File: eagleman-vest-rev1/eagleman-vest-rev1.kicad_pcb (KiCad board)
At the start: 2 copper layers, 84 parts, among them P1 USB_C_Plug_USB2.0, U1 ESP32-S3-WROOM-2, U10 DRV2605LDGSR, U11 DRV2605LDGSR, U12 DRV2605LDGSR, U13 DRV2605LDGSR, U14 DRV2605LDGSR, U15 DRV2605LDGSR, U16 DRV2605LDGSR, U2 AP1117-33, U3 TCA9548APWR, U4 TCA9548APWR, U5 ESP32-S3-WROOM-1-N8, U7 DRV2605LDGSR, U8 DRV2605LDGSR, U9 DRV2605LDGSR

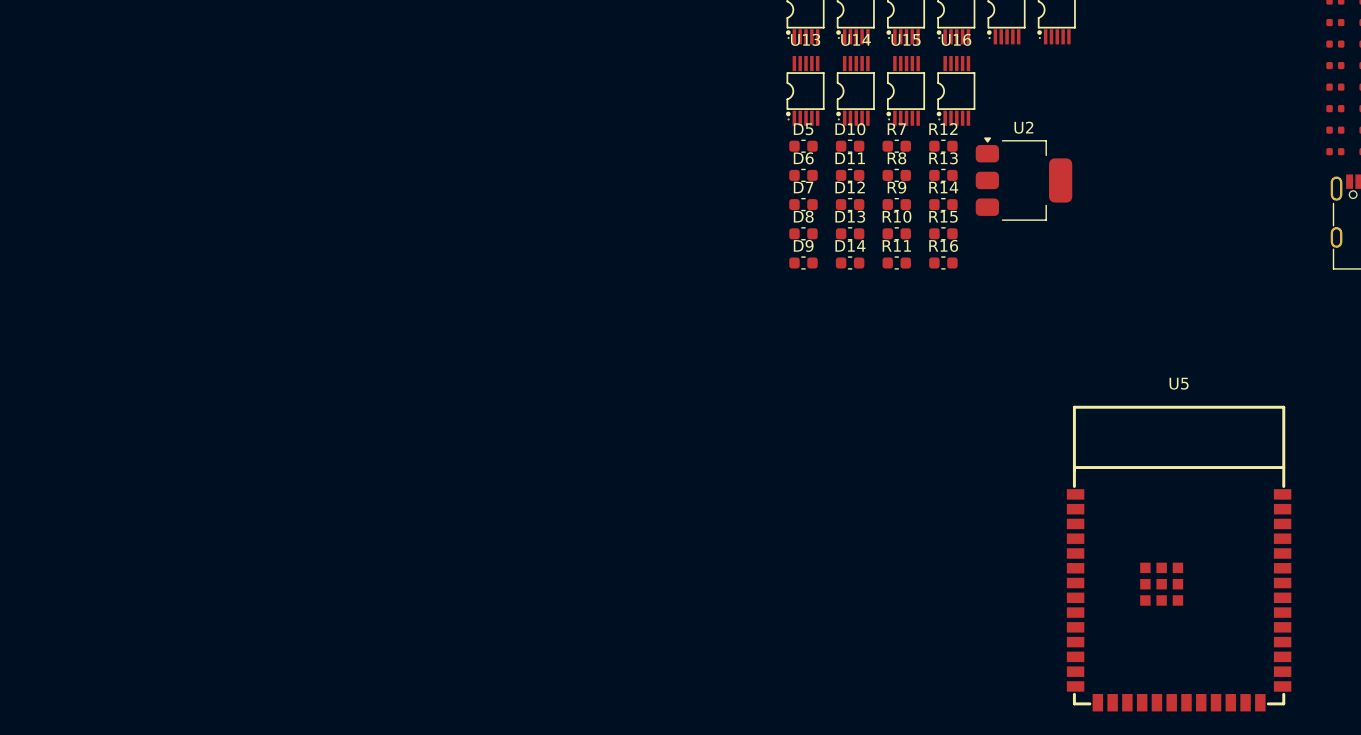
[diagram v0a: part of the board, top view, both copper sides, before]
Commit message: removed duplicate esp32 - why is its footprint not gone?
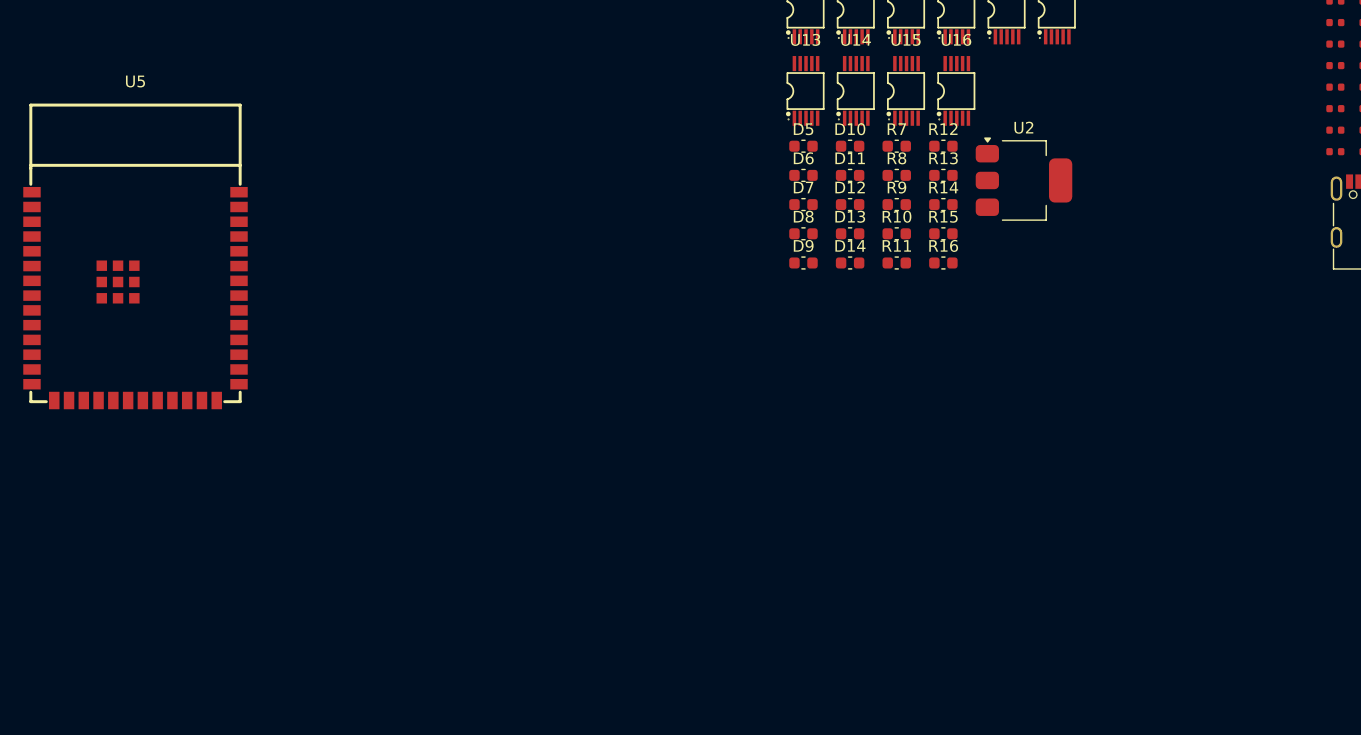
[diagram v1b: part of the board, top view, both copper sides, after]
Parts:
- moved U5 93.4 mm to (70.1, 140.6)
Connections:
- P1 pad A7: Net-(P1-D-) -> Net-(D14-A)
- U1 pad 1: Net-(U1-GND-Pad1) -> GND
- U1 pad 13: Net-(P1-D-) -> Net-(D14-A)
- U1 pad 22: unconnected-(U1-IO14-Pad22) -> /GPIOEN
- U1 pad 23: unconnected-(U1-IO21-Pad23) -> /f1-reset
- U1 pad 31: unconnected-(U1-IO38-Pad31) -> /f2-reset
- U1 pad 40: Net-(U1-GND-Pad1) -> GND
- U1 pad 41: Net-(U1-GND-Pad1) -> GND
- U1 pad 8: unconnected-(U1-IO15-Pad8) -> scl
- U1 pad 9: unconnected-(U1-IO16-Pad9) -> sda
- U3 pad 3: Net-(U3-RESET#) -> /f2-reset
- U4 pad 3: Net-(U4-RESET#) -> /f1-reset

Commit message: started routing
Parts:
- removed D10, D11, D12, D13, D14, D5, D6, D7, D8, D9: LED, Capacitor_SMD:C_0603_1608Metric
- removed R10, R11, R12, R13, R14, R15, R16, R8, R9: 220, Capacitor_SMD:C_0603_1608Metric
- removed U1: ESP32-S3-WROOM-2, RF_Module:ESP32-S3-WROOM-2
- added C14: 100nF, Capacitor_SMD:C_0603_1608Metric, F.Cu at (196.0, 79.0)
- added D31: LED, Capacitor_SMD:C_0603_1608Metric, F.Cu at (137.3, 40.0)
- added D32: LED, Capacitor_SMD:C_0603_1608Metric, F.Cu at (137.3, 42.5)
- added D33: LED, Capacitor_SMD:C_0603_1608Metric, F.Cu at (137.3, 45.0)
- added D34: LED, Capacitor_SMD:C_0603_1608Metric, F.Cu at (137.3, 47.5)
- added D35: LED, Capacitor_SMD:C_0603_1608Metric, F.Cu at (137.3, 50.0)
- added D36: LED, Capacitor_SMD:C_0603_1608Metric, F.Cu at (141.3, 40.0)
- added D37: LED, Capacitor_SMD:C_0603_1608Metric, F.Cu at (141.3, 42.5)
- added D38: LED, Capacitor_SMD:C_0603_1608Metric, F.Cu at (141.3, 45.0)
- added D39: LED, Capacitor_SMD:C_0603_1608Metric, F.Cu at (141.3, 47.5)
- added D40: LED, Capacitor_SMD:C_0603_1608Metric, F.Cu at (141.3, 50.0)
- added J1: Conn_01x08_Pin, Connector_PinHeader_2.54mm:PinHeader_1x08_P2.54mm_Vertical, F.Cu at (220.5, 26.4)
- added J10: Screw_Terminal_01x02, Connector_Phoenix_MC_HighVoltage:PhoenixContact_MCV_1,5_2-G-5.08_1x02_P5.08mm_Vertical, F.Cu at (208.0, 60.6)
- added J11: Screw_Terminal_01x02, Connector_Phoenix_MC_HighVoltage:PhoenixContact_MCV_1,5_2-G-5.08_1x02_P5.08mm_Vertical, F.Cu at (208.0, 49.1)
- added J12: Conn_01x03_Pin, Connector_PinHeader_2.54mm:PinHeader_1x03_P2.54mm_Vertical, F.Cu at (224.5, 31.3)
- added J13: Conn_01x03_Pin, Connector_PinHeader_2.54mm:PinHeader_1x03_P2.54mm_Vertical, F.Cu at (224.5, 35.4)
- added J14: Conn_01x02_Pin, Connector_PinHeader_2.54mm:PinHeader_1x02_P2.54mm_Vertical, F.Cu at (174.5, 58.8)
- added J15: Conn_01x06_Pin, Connector_PinHeader_2.54mm:PinHeader_1x06_P2.54mm_Vertical, F.Cu at (119.5, 34.4)
- added J16: Conn_01x01_Pin, Connector_PinHeader_2.54mm:PinHeader_1x08_P2.54mm_Vertical, F.Cu at (228.8, 26.3)
- added J17: Conn_01x08_Pin, Connector_PinHeader_2.54mm:PinHeader_1x08_P2.54mm_Vertical, F.Cu at (180.0, 83.4)
- added J18: Conn_01x08_Pin, Connector_PinHeader_2.54mm:PinHeader_1x08_P2.54mm_Vertical, F.Cu at (194.5, 101.2)
- added J2: Screw_Terminal_01x02, Connector_Phoenix_MC_HighVoltage:PhoenixContact_MCV_1,5_2-G-5.08_1x02_P5.08mm_Vertical, F.Cu at (208.0, 72.5)
- added J3: Screw_Terminal_01x02, Connector_Phoenix_MC_HighVoltage:PhoenixContact_MCV_1,5_2-G-5.08_1x02_P5.08mm_Vertical, F.Cu at (208.0, 84.0)
- added J4: Screw_Terminal_01x02, Connector_Phoenix_MC_HighVoltage:PhoenixContact_MCV_1,5_2-G-5.08_1x02_P5.08mm_Vertical, F.Cu at (208.0, 96.0)
- added J5: Screw_Terminal_01x02, Connector_Phoenix_MC_HighVoltage:PhoenixContact_MCV_1,5_2-G-5.08_1x02_P5.08mm_Vertical, F.Cu at (166.3, 100.0)
- added J6: Screw_Terminal_01x02, Connector_Phoenix_MC_HighVoltage:PhoenixContact_MCV_1,5_2-G-5.08_1x02_P5.08mm_Vertical, F.Cu at (166.3, 65.5)
- added J7: Screw_Terminal_01x02, Connector_Phoenix_MC_HighVoltage:PhoenixContact_MCV_1,5_2-G-5.08_1x02_P5.08mm_Vertical, F.Cu at (166.3, 54.0)
- added J8: Screw_Terminal_01x02, Connector_Phoenix_MC_HighVoltage:PhoenixContact_MCV_1,5_2-G-5.08_1x02_P5.08mm_Vertical, F.Cu at (166.3, 77.0)
- added J9: Screw_Terminal_01x02, Connector_Phoenix_MC_HighVoltage:PhoenixContact_MCV_1,5_2-G-5.08_1x02_P5.08mm_Vertical, F.Cu at (166.3, 88.8)
- added R53: 220, Capacitor_SMD:C_0603_1608Metric, F.Cu at (145.3, 40.0)
- added R54: 220, Capacitor_SMD:C_0603_1608Metric, F.Cu at (145.3, 42.5)
- added R55: 220, Capacitor_SMD:C_0603_1608Metric, F.Cu at (145.3, 45.0)
- added R56: 220, Capacitor_SMD:C_0603_1608Metric, F.Cu at (145.3, 47.5)
- added R57: 220, Capacitor_SMD:C_0603_1608Metric, F.Cu at (145.3, 50.0)
- added R58: 220, Capacitor_SMD:C_0603_1608Metric, F.Cu at (149.3, 40.0)
- added R59: 220, Capacitor_SMD:C_0603_1608Metric, F.Cu at (149.3, 42.5)
- added R60: 220, Capacitor_SMD:C_0603_1608Metric, F.Cu at (149.3, 45.0)
- added R61: 220, Capacitor_SMD:C_0603_1608Metric, F.Cu at (149.3, 47.5)
- added R62: 220, Capacitor_SMD:C_0603_1608Metric, F.Cu at (149.2, 49.7)
- added SW1: SW_SPST, Button_Switch_SMD:SW_SPST_FSMSM, F.Cu at (225.0, 56.5)
- added SW2: SW_SPST, Button_Switch_SMD:SW_SPST_FSMSM, F.Cu at (196.5, 72.0)
- R7: value 220 -> 10kΩ; footprint Capacitor_SMD:C_0603_1608Metric -> PCM_JLCPCB:R_0402
- U5: value ESP32-S3-WROOM-1-N8 -> ESP32-S3-WROOM-1; footprint TCA9548APWR:WIFIM-SMD_ESP32-S3-WROOM-1-N8 -> RF_Module:ESP32-S3-WROOM-1
- moved U5 146.2 mm to (186.5, 52.1)
- moved U16 94.8 mm to (203.0, 51.5)
- moved U15 89.9 mm to (203.0, 62.5)
- moved U7 85.4 mm to (203.0, 75.5)
- moved R7 79.4 mm to (198.3, 79.0), turned to -90 degrees
- moved R28 79.2 mm to (173.8, 49.4)
- moved U8 76.8 mm to (203.0, 86.5)
- moved R26 76.2 mm to (200.2, 50.5), turned to 180 degrees
- moved R36 74.5 mm to (200.2, 53.5), turned to 180 degrees
- moved U2 73.7 mm to (190.5, 71.5), turned to 90 degrees
- moved C8 71.2 mm to (173.8, 51.4)
- moved C11 70.8 mm to (200.2, 62.7), turned to 180 degrees
- moved C27 70.4 mm to (173.8, 50.4)
- moved C24 69.9 mm to (200.2, 51.5), turned to 180 degrees
- moved U9 68.7 mm to (203.0, 99.0)
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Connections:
- C1 pad 2: GNDREF -> GND
- C2 pad 2: GNDREF -> GND
- P1 pad A7: Net-(D14-A) -> Net-(P1-D-)
- R7 pad 1: Net-(D5-A) -> +3.3V
- R7 pad 2: Net-(U1-IO1) -> /EN_PIN
- U2 pad 1: GNDREF -> GND
- U3 pad 10: /f2-sd3 -> Net-(J18-Pin_3)
- U3 pad 11: /f2-sc3 -> Net-(J18-Pin_4)
- U3 pad 13: /f2-sd4 -> Net-(J17-Pin_1)
- U3 pad 14: /f2-sc4 -> Net-(J17-Pin_2)
- U3 pad 15: /f2-sd5 -> Net-(J17-Pin_3)
- U3 pad 16: /f2-sc5 -> Net-(J17-Pin_4)
- U3 pad 17: /f2-sd6 -> Net-(J17-Pin_5)
- U3 pad 18: /f2-sc6 -> Net-(J17-Pin_6)
- U3 pad 19: /f2-sd7 -> Net-(J17-Pin_7)
- U3 pad 20: /f2-sc7 -> Net-(J17-Pin_8)
- U3 pad 8: /f2-sd2 -> Net-(J18-Pin_1)
- U3 pad 9: /f2-sc2 -> Net-(J18-Pin_2)
- U5 pad 10: unconnected-(U5-IO17-Pad10) -> Net-(J14-Pin_2)
- U5 pad 11: unconnected-(U5-IO18-Pad11) -> Net-(J14-Pin_1)
- U5 pad 12: unconnected-(U5-IO8-Pad12) -> sda
- U5 pad 13: unconnected-(U5-IO19-Pad13) -> Net-(P1-D-)
- U5 pad 14: unconnected-(U5-IO20-Pad14) -> Net-(P1-D+)
- U5 pad 15: unconnected-(U5-IO3-Pad15) -> Net-(J13-Pin_3)
- U5 pad 16: unconnected-(U5-IO46-Pad16) -> Net-(J12-Pin_1)
- U5 pad 17: unconnected-(U5-IO9-Pad17) -> scl
- U5 pad 18: unconnected-(U5-IO10-Pad18) -> /GPIOEN
- U5 pad 19: unconnected-(U5-IO11-Pad19) -> Net-(U5-IO11)
- U5 pad 20: unconnected-(U5-IO12-Pad20) -> Net-(U5-IO12)
- U5 pad 21: unconnected-(U5-IO13-Pad21) -> Net-(U5-IO13)
- U5 pad 22: unconnected-(U5-IO14-Pad22) -> Net-(U5-IO14)
- U5 pad 23: unconnected-(U5-IO21-Pad23) -> Net-(J1-Pin_8)
- U5 pad 24: unconnected-(U5-IO47-Pad24) -> /f1-reset
- U5 pad 25: unconnected-(U5-IO48-Pad25) -> /f2-reset
- U5 pad 26: unconnected-(U5-IO45-Pad26) -> Net-(J12-Pin_2)
- U5 pad 27: unconnected-(U5-IO0-Pad27) -> /BOOT_PIN
- U5 pad 28: unconnected-(U5-IO35-Pad28) -> Net-(J1-Pin_7)
- U5 pad 29: unconnected-(U5-IO36-Pad29) -> Net-(J1-Pin_6)
- U5 pad 3: unconnected-(U5-EN-Pad3) -> /EN_PIN
- U5 pad 30: unconnected-(U5-IO37-Pad30) -> Net-(J1-Pin_5)
- U5 pad 31: unconnected-(U5-IO38-Pad31) -> Net-(J1-Pin_4)
- U5 pad 32: unconnected-(U5-IO39-Pad32) -> Net-(J1-Pin_3)
- U5 pad 33: unconnected-(U5-IO40-Pad33) -> Net-(J1-Pin_2)
- U5 pad 34: unconnected-(U5-IO41-Pad34) -> Net-(J1-Pin_1)
- U5 pad 35: unconnected-(U5-IO42-Pad35) -> Net-(J12-Pin_3)
- U5 pad 36: unconnected-(U5-RXD0-Pad36) -> /rx
- U5 pad 37: unconnected-(U5-TXD0-Pad37) -> /tx
- U5 pad 38: unconnected-(U5-IO2-Pad38) -> Net-(J13-Pin_2)
- U5 pad 39: unconnected-(U5-IO1-Pad39) -> Net-(J13-Pin_1)
- U5 pad 40: unconnected-(U5-GND-Pad40) -> GND
- U5 pad 41: unconnected-(U5-EP-Pad41) -> GND
- U5 pad 6: unconnected-(U5-IO6-Pad6) -> Net-(U5-IO6)
- U5 pad 7: /GPIOEN -> Net-(U5-IO7)
- U5 pad 8: scl -> Net-(U5-IO15)
- U5 pad 9: sda -> Net-(U5-IO16)
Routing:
- net GND: track 0.00 -> 17.3 mm
- net Net-(J18-Pin_1): track 0.00 -> 12.1 mm
- net Net-(J18-Pin_2): track 0.00 -> 10.3 mm
- net Net-(J17-Pin_8): track 0.00 -> 10.0 mm
- net Net-(J9-Pin_1): track 0.00 -> 8.56 mm
- net Net-(J18-Pin_3): track 0.00 -> 8.41 mm
- net Net-(J9-Pin_2): track 0.00 -> 8.40 mm
- net Net-(J17-Pin_7): track 0.00 -> 8.14 mm
- net Net-(J5-Pin_1): track 0.00 -> 8.00 mm
- net Net-(J5-Pin_2): track 0.00 -> 7.96 mm
- net Net-(J17-Pin_1): track 0.00 -> 7.76 mm
- net Net-(J11-Pin_2): track 0.00 -> 7.65 mm
- net Net-(J6-Pin_1): track 0.00 -> 7.54 mm
- net Net-(J10-Pin_2): track 0.00 -> 7.35 mm
- net Net-(J8-Pin_1): track 0.00 -> 7.34 mm
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
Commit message: fixed up, might still be too dense
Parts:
- moved J16 103.3 mm to (181.3, 118.0), turned to -90 degrees
- moved J12 94.9 mm to (186.0, 118.0), turned to 90 degrees
- moved J13 85.5 mm to (191.0, 114.0), turned to -90 degrees
- moved D31 73.7 mm to (180.8, 99.5)
- moved D32 73.7 mm to (180.8, 102.0)
- moved D34 73.7 mm to (180.8, 107.0)
- moved D35 73.7 mm to (180.8, 109.5)
- moved D36 73.7 mm to (184.8, 99.5)
- moved D37 73.7 mm to (184.8, 102.0)
- moved D39 73.7 mm to (184.8, 107.0)
- moved D40 73.7 mm to (184.8, 109.5)
- moved R53 73.7 mm to (188.8, 99.5)
- moved R54 73.7 mm to (188.8, 102.0)
- moved R56 73.7 mm to (188.8, 107.0)
- moved R57 73.7 mm to (188.8, 109.5)
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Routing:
- net GND: track 17.3 -> 1.34 mm
- net Net-(J13-Pin_3): track 0.00 -> 0.80 mm

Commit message: more updates
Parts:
- moved C27 19.0 mm to (157.5, 53.5)
- moved C8 19.0 mm to (157.5, 54.5)
- moved R28 19.0 mm to (157.5, 52.5)
- moved R3 19.0 mm to (157.5, 57.0)
- moved R5 19.0 mm to (157.5, 56.0)
- moved C1 18.8 mm to (222.2, 56.4)
- moved C14 18.8 mm to (228.2, 59.8)
- moved C2 18.8 mm to (217.2, 56.4)
- moved R7 18.8 mm to (219.8, 56.4)
- moved SW1 18.8 mm to (227.2, 51.5)
- moved SW2 18.8 mm to (221.2, 60.0)
- moved U2 18.8 mm to (219.2, 50.5)
- moved R24 16.1 mm to (173.5, 102.8)
- moved J1 14.3 mm to (198.2, 47.3)
- moved R34 14.1 mm to (173.5, 101.8)
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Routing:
- net Net-(U5-IO15): track 0.00 -> 56.8 mm, vias 0 -> 4
- net Net-(U5-IO4): track 0.00 -> 53.5 mm, vias 0 -> 1
- net Net-(U5-IO5): track 0.00 -> 53.1 mm, vias 0 -> 1
- net Net-(U5-IO16): track 0.00 -> 51.0 mm, vias 0 -> 1
- net Net-(U5-IO7): track 0.00 -> 49.1 mm, vias 0 -> 1
- net Net-(J1-Pin_1): track 0.00 -> 13.7 mm
- net Net-(J1-Pin_8): track 0.00 -> 10.0 mm
- net Net-(J9-Pin_2): track 8.40 -> 0.00 mm
- net Net-(J1-Pin_2): track 0.00 -> 7.70 mm
- net Net-(J10-Pin_2): track 7.35 -> 0.00 mm
- net Net-(J6-Pin_2): track 7.25 -> 0.00 mm
- net Net-(J6-Pin_1): track 7.54 -> 0.34 mm
- net Net-(J2-Pin_1): track 7.07 -> 0.00 mm
- net Net-(J10-Pin_1): track 7.05 -> 0.00 mm
- net Net-(J7-Pin_1): track 6.79 -> 0.00 mm
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
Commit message: i need help
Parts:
- moved R28 33.1 mm to (182.2, 74.5), turned to 180 degrees
- moved R3 23.7 mm to (177.8, 69.2), turned to -90 degrees
- moved R5 23.2 mm to (177.8, 67.2), turned to 90 degrees
- moved C10 21.8 mm to (173.5, 103.8)
- moved SW1 21.6 mm to (206.2, 56.5), turned to 180 degrees
- moved C8 20.9 mm to (173.2, 68.2), turned to -90 degrees
- moved C14 20.5 mm to (209.5, 51.5)
- moved R32 18.8 mm to (173.0, 113.8), turned to -90 degrees
- moved C27 18.7 mm to (175.0, 47.0)
- moved C6 18.1 mm to (171.8, 113.8), turned to -90 degrees
- moved R22 15.6 mm to (175.0, 113.8), turned to -90 degrees
- moved U2 15.3 mm to (204.0, 50.0)
- moved SW2 14.9 mm to (206.2, 60.5), turned to 180 degrees
- moved C1 14.7 mm to (209.5, 49.0)
- moved R7 12.7 mm to (208.2, 51.0), turned to 90 degrees
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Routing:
- net Net-(J13-Pin_3): track 0.80 -> 88.2 mm
- net Net-(J13-Pin_2): track 0.00 -> 79.4 mm
- net Net-(J13-Pin_1): track 0.00 -> 69.9 mm, vias 0 -> 3
- net Net-(J12-Pin_1): track 0.00 -> 68.4 mm
- net /EN_PIN: track 0.00 -> 67.9 mm
- net Net-(J12-Pin_3): track 0.00 -> 66.3 mm
- net Net-(J12-Pin_2): track 0.00 -> 56.0 mm
- net Net-(J15-Pin_6): track 0.00 -> 54.8 mm
- net /f1-sd3: track 0.00 -> 51.9 mm, vias 0 -> 1
- net /GPIOEN: track 0.00 -> 42.5 mm, vias 0 -> 5
- net +5V: track 0.16 -> 27.1 mm, vias 0 -> 1
- net /f1-sd5: track 0.00 -> 23.2 mm, vias 0 -> 1
- net /f1-sc3: track 0.00 -> 20.3 mm, vias 0 -> 1
- net Net-(J8-Pin_2): track 1.09 -> 21.3 mm
- net Net-(J6-Pin_1): track 0.34 -> 17.2 mm
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
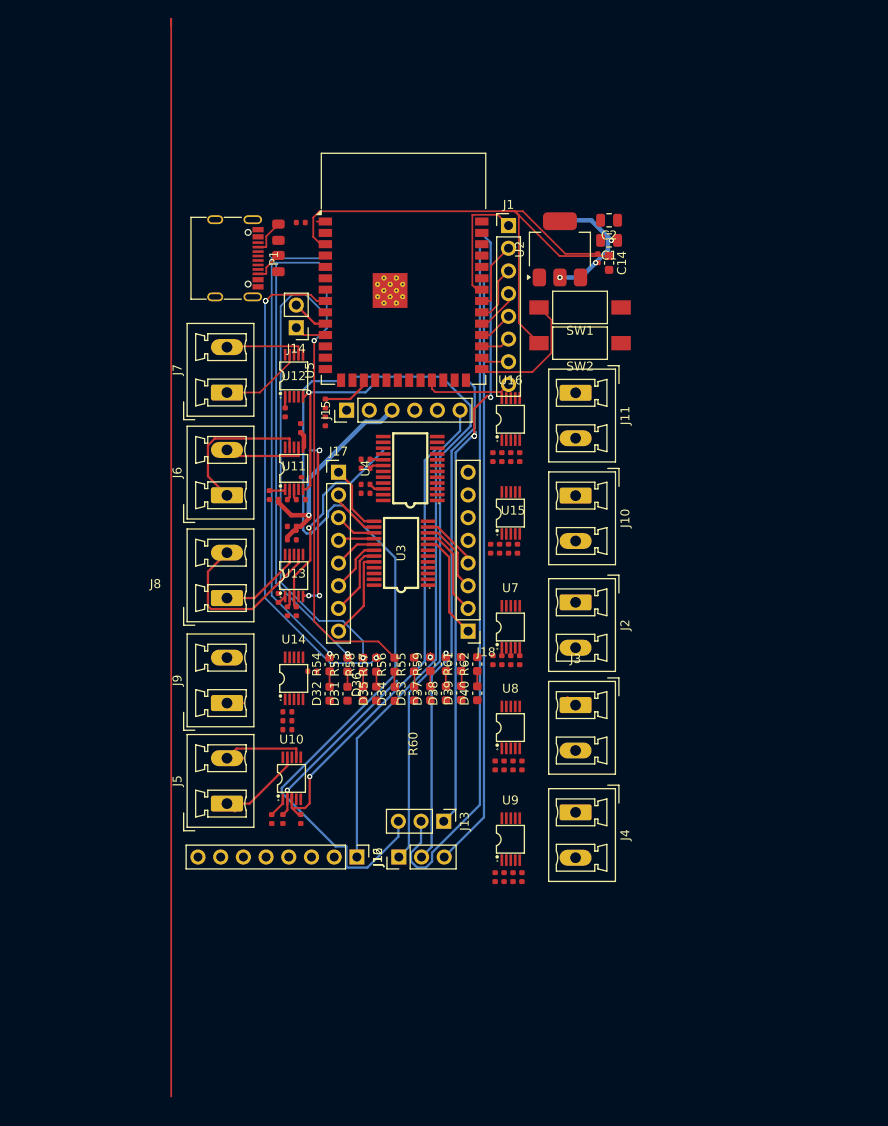
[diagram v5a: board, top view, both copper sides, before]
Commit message: updated routing and lowered density a little bit
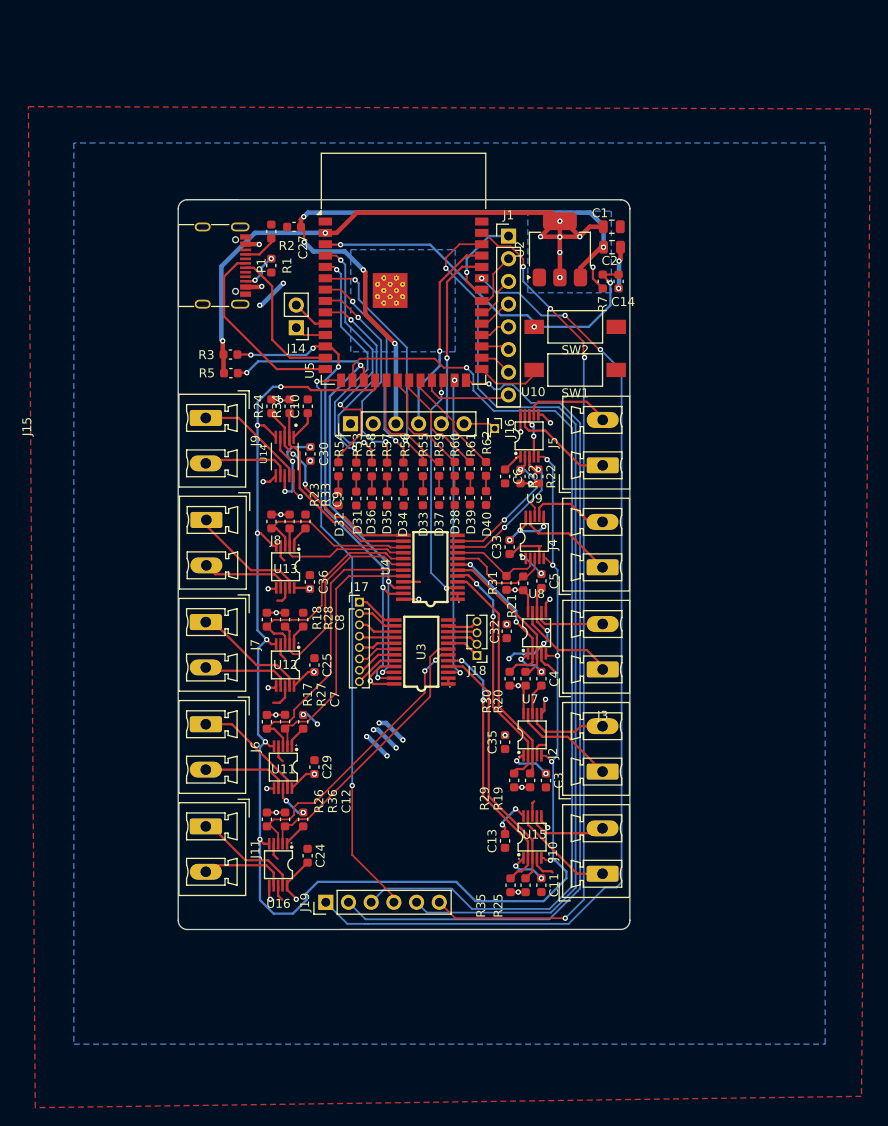
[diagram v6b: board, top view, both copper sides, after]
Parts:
- removed J12, J13: Conn_01x03_Pin, Connector_PinHeader_2.54mm:PinHeader_1x03_P2.54mm_Vertical
- removed R4, R6: 4.7kΩ, PCM_JLCPCB:R_0402
- added J19: Conn_01x06_Pin, Connector_PinHeader_2.54mm:PinHeader_1x06_P2.54mm_Vertical, F.Cu at (177.8, 123.1)
- C10, C11, C12, C13, C24, C25, C27, C29, C3, C30, C32, C33, C35, C36, C4, C5, C6, C7, C8, C9: footprint PCM_JLCPCB:C_0402 -> Capacitor_SMD:C_0603_1608Metric
- J16: footprint Connector_PinHeader_2.54mm:PinHeader_1x08_P2.54mm_Vertical -> Connector_PinHeader_1.27mm:PinHeader_1x01_P1.27mm_Vertical
- J17: footprint Connector_PinHeader_2.54mm:PinHeader_1x08_P2.54mm_Vertical -> Connector_PinHeader_1.27mm:PinHeader_1x08_P1.27mm_Vertical
- J18: value Conn_01x08_Pin -> Conn_01x04_Pin; footprint Connector_PinHeader_2.54mm:PinHeader_1x08_P2.54mm_Vertical -> Connector_PinHeader_1.27mm:PinHeader_1x04_P1.27mm_Vertical
- R1, R2: footprint PCM_JLCPCB:R_0805 -> Capacitor_SMD:C_0603_1608Metric
- R17, R18, R19, R20, R21, R22, R23, R24, R25, R26, R27, R28, R29, R3, R30, R31, R32, R33, R34, R35, R36, R5, R7: footprint PCM_JLCPCB:R_0402 -> Capacitor_SMD:C_0603_1608Metric
- U14: footprint TCA9548APWR:driver_footprint_maybe -> DRV2605:SOP50P490X110-10N
- moved J11 63.8 mm to (164.4, 114.6)
- moved J5 56.6 mm to (208.8, 74.2)
- moved U16 56.3 mm to (172.5, 118.9), turned to 180 degrees
- moved J16 50.4 mm to (196.7, 70.1)
- moved C24 49.6 mm to (175.8, 117.9)
- moved R36 48.3 mm to (173.2, 113.8), turned to 90 degrees
- moved R26 47.8 mm to (171.2, 113.8), turned to 90 degrees
- moved C12 46.7 mm to (175.3, 113.8), turned to 90 degrees
- moved R22 46.7 mm to (201.6, 75.4)
- moved R32 46.7 mm to (199.6, 75.4)
- moved U10 46.7 mm to (200.6, 70.9)
- moved C6 46.4 mm to (197.9, 75.4)
- moved J10 42.4 mm to (208.8, 119.9), turned to 90 degrees
- moved C11 37.9 mm to (201.9, 121.1)
- moved R25 37.9 mm to (200.2, 121.2)
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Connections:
- U15 pad 4: unconnected-(U15-IN/TRIG-Pad4) -> GND
- U5 pad 15: Net-(J13-Pin_3) -> /p3
- U5 pad 16: Net-(J12-Pin_1) -> /p46
- U5 pad 26: Net-(J12-Pin_2) -> /p45
- U5 pad 35: Net-(J12-Pin_3) -> /p42
- U5 pad 38: Net-(J13-Pin_2) -> /p2
- U5 pad 39: Net-(J13-Pin_1) -> /p1
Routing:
- net /GPIOEN: track 42.5 -> 175.3 mm, vias 5 -> 11
- net +5V: track 27.1 -> 151.2 mm, vias 1 -> 42
- net /p42: track 0.00 -> 113.2 mm, vias 0 -> 3
- net /p46: track 0.00 -> 107.2 mm, vias 0 -> 1
- net /p2: track 0.00 -> 104.6 mm, vias 0 -> 1
- net /p1: track 0.00 -> 98.9 mm, vias 0 -> 4
- net /p45: track 0.00 -> 95.4 mm, vias 0 -> 1
- net GND: track 1.34 -> 93.7 mm, vias 0 -> 22
- net Net-(J13-Pin_3): track 88.2 -> 0.00 mm
- net Net-(J13-Pin_2): track 79.4 -> 0.00 mm
- net Net-(J13-Pin_1): track 69.9 -> 0.00 mm, vias 3 -> 0
- net Net-(J12-Pin_1): track 68.4 -> 0.00 mm
- net Net-(J12-Pin_3): track 66.3 -> 0.00 mm
- net /p3: track 0.00 -> 64.6 mm, vias 0 -> 2
- net +3.3V: track 16.0 -> 75.8 mm, vias 3 -> 9
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- added copper zone on B.Cu, net +3.3V
- added copper zone on B.Cu, net +5V
- added copper zone on B.Cu, net GND
- added copper zone on F.Cu, net GND
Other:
- board outline added: 50.5 x 81.7 mm
